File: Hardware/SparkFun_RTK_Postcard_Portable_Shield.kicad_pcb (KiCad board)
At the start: 2 copper layers, 43.2 x 43.2 mm, 92 parts, among them J1 microSD_Friction, J10 Conn_01x06, J2 Conn_01x05, J3 JST_2mm_LiPo, J4 I2C, J5 Conn_01x04, SW2 Nav Switch, U1 AP2112K-3.3, U2 MAX17048, U3 MCP73831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

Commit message: Add ignore.
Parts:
- removed kibuzzard-66CAA426 (x2): G***, kibuzzard-66CAA426
- removed kibuzzard-66CAA9AE: G***, kibuzzard-66CAA9AE
- removed kibuzzard-66F080A6: G***, kibuzzard-66F080A6

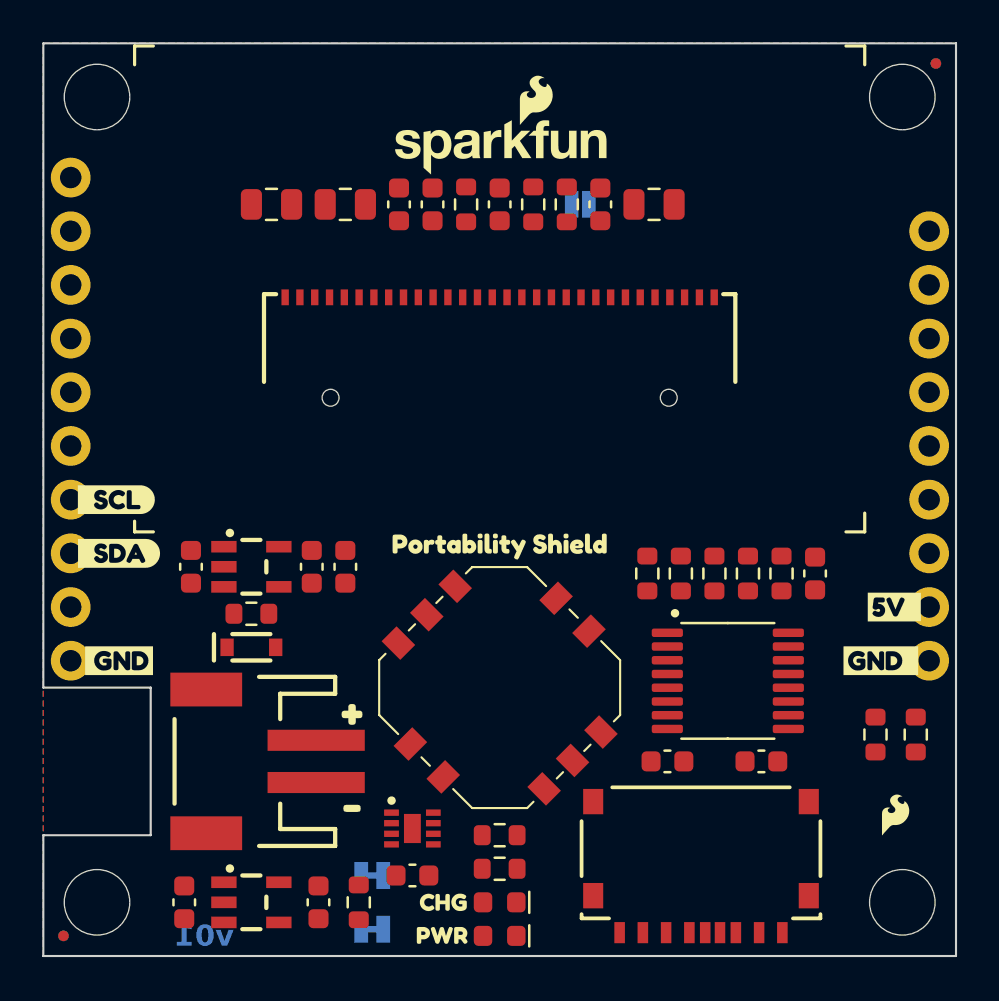
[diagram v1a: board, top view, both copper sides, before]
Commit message: Change to dedicated header format.
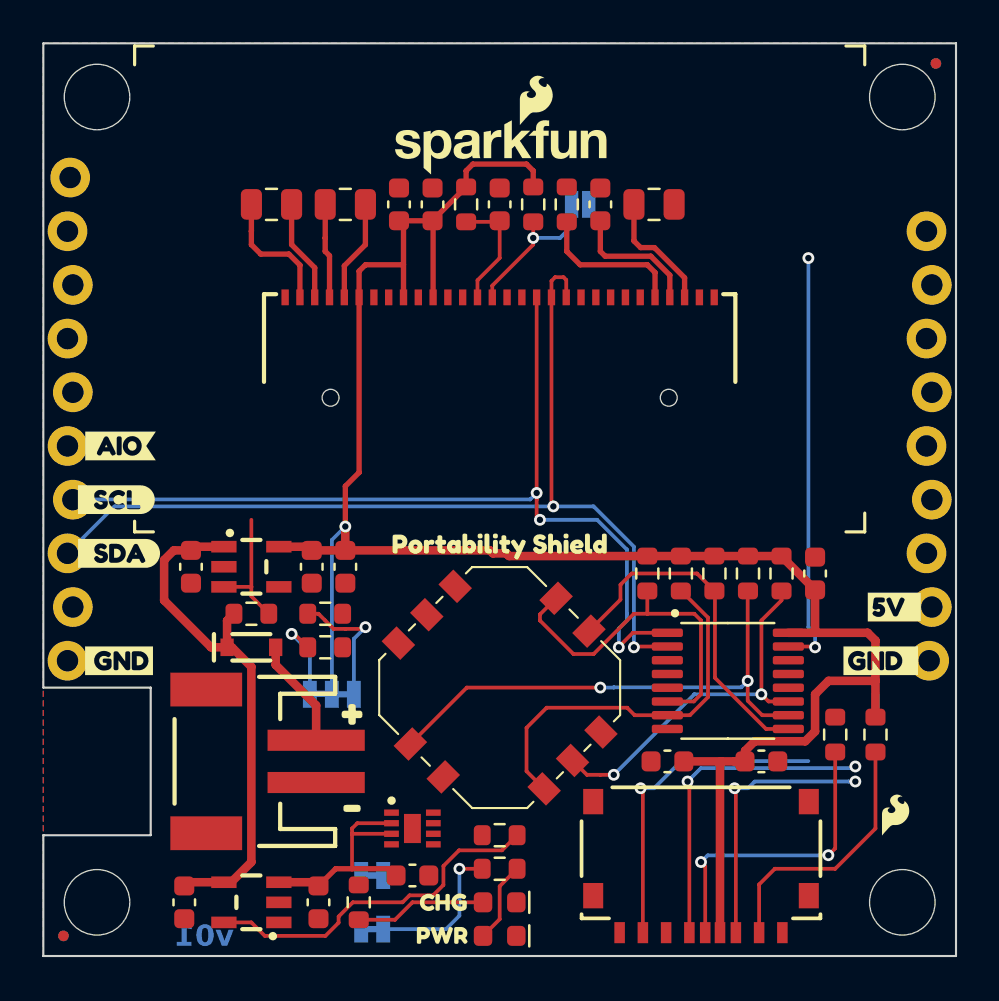
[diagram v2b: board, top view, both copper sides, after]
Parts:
- removed J10: Conn_01x06, SparkFun-Connector:1x06
- removed J5: Conn_01x04, SparkFun-Connector:1x04
- added JP4: I²C, SparkFun-Jumper:Jumper_3_NC-2_Trace, B.Cu at (148.9, 105.1)
- added R15: 2.2k, SparkFun-Resistor:R_0603_1608Metric, F.Cu at (148.6, 102.9)
- added R16: 2.2k, SparkFun-Resistor:R_0603_1608Metric, F.Cu at (148.6, 101.3)
- added kibuzzard-66F377AE: G***, kibuzzard-66F377AE, F.Cu at (138.9, 93.3)
- added kibuzzard-66F37954: G***, kibuzzard-66F37954, B.Cu at (151.9, 105.1)
- added kibuzzard-66F3797E: G***, kibuzzard-66F3797E, B.Cu at (138.9, 93.3)
- J2: value Conn_01x05 -> 1x10; footprint SparkFun-Connector:1x05 -> SparkFun-Connector:1x10_Locking; moved to F.Cu
- J4: value I2C -> 1x09; footprint SparkFun-Connector:1x04 -> SparkFun-Connector:1x09_Locking; moved to F.Cu
- R13: value 10k -> 100k
- moved J2 42.6 mm to (136.5, 80.6)
- moved J4 40.6 mm to (177.2, 103.5)
- moved R6 3.81 mm to (172.7, 107.0)
- moved R10 1.59 mm to (167.0, 99.4)
- moved R11 1.59 mm to (168.6, 99.4)
- turned C4 to -90 degrees
- turned C5 to -90 degrees
- turned C9 to -90 degrees
- turned JP2 to 180 degrees
- turned U3 to 180 degrees
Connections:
- C6 pad 1: Net-(U5-~{RESET}) -> ~{RESET}_P
- J2 pad 1: Main-TX -> unconnected-(J2-Pin_1-Pad1)
- J2 pad 2: Main-RX -> 3V3_EN
- J2 pad 4: 5V -> unconnected-(J2-Pin_4-Pad4)
- J2 pad 5: GND -> unconnected-(J2-Pin_5-Pad5)
- J4 pad 2: unconnected-(J4-Pin_2-Pad2) -> 5V
- J4 pad 3: SDA -> unconnected-(J4-Pin_7-Pad3)
- J4 pad 4: SCL -> Main-RX
- R1 pad 1: Net-(U5-~{RESET}) -> ~{RESET}_P
- U4 pad 12: SD_CD -> unconnected-(U4-IO5-Pad12)
- U4 pad 15: 3.3V_P -> ~{RESET}_P
- U5 pad 14: Net-(U5-~{RESET}) -> ~{RESET}_P
- U5 pad 21: unconnected-(U5-D3-Pad21) -> GND
- U5 pad 22: unconnected-(U5-D4-Pad22) -> GND
- U5 pad 23: unconnected-(U5-D5-Pad23) -> GND
- U5 pad 24: unconnected-(U5-D6-Pad24) -> GND
- U5 pad 25: unconnected-(U5-D7-Pad25) -> GND
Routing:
- net 3.3V_P: track 0.00 -> 97.3 mm, vias 0 -> 1
- net SDA: track 0.00 -> 47.2 mm, vias 0 -> 2
- net SCL: track 0.00 -> 44.7 mm, vias 0 -> 3
- net ~{RESET}_P: track 0.00 -> 25.5 mm, vias 0 -> 2
- net 5V: track 0.00 -> 25.0 mm
- net SW_Left: track 0.00 -> 24.6 mm, vias 0 -> 2
- net SW_Down: track 0.00 -> 18.3 mm
- net SW_Center: track 0.00 -> 17.5 mm, vias 0 -> 2
- net VBATT: track 0.00 -> 17.0 mm
- net SW_Up: track 0.00 -> 16.9 mm
- net Net-(U3-PROG): track 0.00 -> 16.8 mm
- net SW_Right: track 0.00 -> 16.4 mm
- net SHLD_SCK: track 0.00 -> 15.5 mm, vias 0 -> 2
- net SHLD_POCI: track 0.00 -> 15.3 mm, vias 0 -> 1
- net SD_CD: track 0.00 -> 14.6 mm, vias 0 -> 2
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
